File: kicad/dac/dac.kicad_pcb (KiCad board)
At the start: 4 copper layers, 100 x 99 mm, 58 parts, among them J1 USB_C_Receptacle_USB2.0, Q1 PNP, Q11 NPN, Q12 PNP, Q15 NPN, Q19 NPN, Q2 PNP, Q20 PNP, Q3 PNP, Q4 PNP, Q7 NPN, U1 PCM2704/4C/5/5C

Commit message: Commit
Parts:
- removed C1, C4, C6: 1u, Capacitor_SMD:C_0805_2012Metric_Pad1.18x1.45mm_HandSolder
- removed Q1: PNP, Package_TO_SOT_THT:TO-92L_Inline
- removed R33: 234, Resistor_THT:R_Axial_DIN0207_L6.3mm_D2.5mm_P10.16mm_Horizontal
- removed R6: R, Resistor_SMD:R_0805_2012Metric_Pad1.20x1.40mm_HandSolder
- added C10: 100n, Capacitor_SMD:C_1206_3216Metric_Pad1.33x1.80mm_HandSolder, F.Cu at (173.3, 74.0)
- added C11: 20n, Capacitor_SMD:C_1206_3216Metric_Pad1.33x1.80mm_HandSolder, F.Cu at (173.3, 77.3)
- added C12: 20n, Capacitor_SMD:C_1206_3216Metric_Pad1.33x1.80mm_HandSolder, F.Cu at (173.3, 80.7)
- added C13: 10u, Capacitor_SMD:C_1206_3216Metric_Pad1.33x1.80mm_HandSolder, F.Cu at (173.3, 84.0)
- added C14: 10u, Capacitor_SMD:C_1206_3216Metric_Pad1.33x1.80mm_HandSolder, F.Cu at (173.3, 87.4)
- added C18: 30pF, Capacitor_SMD:C_1206_3216Metric_Pad1.33x1.80mm_HandSolder, F.Cu at (159.1, 74.6)
- added C19: 10u, Capacitor_THT:CP_Radial_D5.0mm_P2.50mm, F.Cu at (139.3, 105.1)
- added C26: 30pF, Capacitor_SMD:C_1206_3216Metric_Pad1.33x1.80mm_HandSolder, F.Cu at (159.1, 19.6)
- added C27: 10u, Capacitor_THT:CP_Radial_D5.0mm_P2.50mm, F.Cu at (126.2, 44.9)
- added C3: 2u2, Capacitor_SMD:C_1206_3216Metric_Pad1.33x1.80mm_HandSolder, F.Cu at (173.3, 60.6)
- added C7: 100n, Capacitor_SMD:C_1206_3216Metric_Pad1.33x1.80mm_HandSolder, F.Cu at (173.3, 67.3)
- added C8: 2u2, Capacitor_SMD:C_1206_3216Metric_Pad1.33x1.80mm_HandSolder, F.Cu at (173.3, 70.6)
- added Q10: PNP, Package_SO:SC-74-6_1.5x2.9mm_P0.95mm, F.Cu at (165.2, 66.7)
- added Q16: PNP, Package_TO_SOT_THT:TO-220-3_Vertical, F.Cu at (158.3, 108.2)
- added Q17: PNP, Package_SO:SC-74-6_1.5x2.9mm_P0.95mm, F.Cu at (165.2, 2.80)
- added Q18: PNP, Package_SO:TSOP-6_1.65x3.05mm_P0.95mm, F.Cu at (164.3, 20.2)
- added Q21: PNP, Package_SO:SC-74-6_1.5x2.9mm_P0.95mm, F.Cu at (165.2, 11.7)
- added Q22: NPN, Package_TO_SOT_THT:TO-92, F.Cu at (158.0, 9.62)
- added Q23: NPN, Package_TO_SOT_THT:TO-92, F.Cu at (158.0, 15.4)
- added Q26: NPN, Package_TO_SOT_THT:TO-220-3_Vertical, F.Cu at (115.7, 45.5)
- added Q27: PNP, Package_TO_SOT_THT:TO-220-3_Vertical, F.Cu at (115.7, 51.5)
- added Q5: PNP, Package_TO_SOT_THT:TO-92, F.Cu at (178.3, 92.6)
- added Q6: PNP, Package_SO:SC-74-6_1.5x2.9mm_P0.95mm, F.Cu at (165.2, 57.8)
- added Q8: NPN, Package_SO:SC-74-6_1.5x2.9mm_P0.95mm, F.Cu at (165.2, 62.2)
- added Q9: NPN, Package_TO_SOT_THT:TO-92, F.Cu at (158.0, 58.8)
- added R27: 2k, Resistor_THT:R_Axial_DIN0207_L6.3mm_D2.5mm_P10.16mm_Horizontal, F.Cu at (156.6, 92.2)
- added R28: 20k, Resistor_THT:R_Axial_DIN0207_L6.3mm_D2.5mm_P10.16mm_Horizontal, F.Cu at (156.6, 96.3)
- added R41: 68, Resistor_THT:R_Axial_DIN0207_L6.3mm_D2.5mm_P10.16mm_Horizontal, F.Cu at (156.6, 29.1)
- added R42: 20k, Resistor_THT:R_Axial_DIN0207_L6.3mm_D2.5mm_P10.16mm_Horizontal, F.Cu at (156.6, 33.2)
- added R43: 27k, Resistor_SMD:R_1206_3216Metric_Pad1.30x1.75mm_HandSolder, F.Cu at (140.2, 28.8)
- added R44: 470, Resistor_SMD:R_1206_3216Metric_Pad1.30x1.75mm_HandSolder, F.Cu at (140.2, 32.1)
- added R45: 430, Resistor_SMD:R_1206_3216Metric_Pad1.30x1.75mm_HandSolder, F.Cu at (140.2, 35.4)
- added R46: 68, Resistor_SMD:R_1206_3216Metric_Pad1.30x1.75mm_HandSolder, F.Cu at (140.2, 38.6)
- added R47: 680, Resistor_SMD:R_1206_3216Metric_Pad1.30x1.75mm_HandSolder, F.Cu at (140.2, 41.9)
- added R48: 68, Resistor_SMD:R_1206_3216Metric_Pad1.30x1.75mm_HandSolder, F.Cu at (140.2, 45.2)
- added R49: 430, Resistor_SMD:R_1206_3216Metric_Pad1.30x1.75mm_HandSolder, F.Cu at (146.1, 28.8)
- added R50: 470, Resistor_SMD:R_1206_3216Metric_Pad1.30x1.75mm_HandSolder, F.Cu at (146.1, 32.1)
- added R51: 2k, Resistor_THT:R_Axial_DIN0207_L6.3mm_D2.5mm_P10.16mm_Horizontal, F.Cu at (156.6, 37.2)
- added R52: 20k, Resistor_THT:R_Axial_DIN0207_L6.3mm_D2.5mm_P10.16mm_Horizontal, F.Cu at (156.6, 41.3)
- added R53: 27k, Resistor_SMD:R_1206_3216Metric_Pad1.30x1.75mm_HandSolder, F.Cu at (146.1, 35.4)
- added R54: 2k2, Resistor_SMD:R_1206_3216Metric_Pad1.30x1.75mm_HandSolder, F.Cu at (146.1, 38.6)
- added R55: 2k2, Resistor_SMD:R_1206_3216Metric_Pad1.30x1.75mm_HandSolder, F.Cu at (146.1, 41.9)
- added R56: 680, Resistor_SMD:R_1206_3216Metric_Pad1.30x1.75mm_HandSolder, F.Cu at (146.1, 45.2)
- added R58: 68, Resistor_SMD:R_1206_3216Metric_Pad1.30x1.75mm_HandSolder, F.Cu at (152.1, 28.8)
- added R59: 100, Resistor_SMD:R_1206_3216Metric_Pad1.30x1.75mm_HandSolder, F.Cu at (152.1, 32.1)
- added R60: 22, Resistor_SMD:R_1206_3216Metric_Pad1.30x1.75mm_HandSolder, F.Cu at (152.1, 35.4)
- added R61: 33, Resistor_SMD:R_1206_3216Metric_Pad1.30x1.75mm_HandSolder, F.Cu at (152.1, 38.6)
- added R62: 33, Resistor_SMD:R_1206_3216Metric_Pad1.30x1.75mm_HandSolder, F.Cu at (152.1, 41.9)
- added R63: 1, Resistor_THT:R_Axial_DIN0614_L14.3mm_D5.7mm_P20.32mm_Horizontal, F.Cu at (114.7, 30.8)
- added R64: 1, Resistor_THT:R_Axial_DIN0614_L14.3mm_D5.7mm_P20.32mm_Horizontal, F.Cu at (114.7, 38.0)
- C2: value 1u -> 100n; footprint Capacitor_SMD:C_0805_2012Metric_Pad1.18x1.45mm_HandSolder -> Capacitor_SMD:C_1206_3216Metric_Pad1.33x1.80mm_HandSolder
- C5: value 1u -> 2u2; footprint Capacitor_SMD:C_0805_2012Metric_Pad1.18x1.45mm_HandSolder -> Capacitor_SMD:C_1206_3216Metric_Pad1.33x1.80mm_HandSolder
- HS1, HS2: footprint Heatsink:Heatsink_Fischer_SK104-STCB_35x13mm__2xDrill3.5mm_ScrewM3 -> Heatsink:Heatsink_Fischer_SK129-STS_42x25mm_2xDrill2.5mm
- J1: value USB_C_Receptacle_USB2.0 -> Conn_01x09_Pin; footprint Connector_USB:USB_C_Receptacle_GCT_USB4085 -> Connector_PinHeader_2.54mm:PinHeader_1x09_P2.54mm_Vertical
- Q11: footprint Package_TO_SOT_THT:TO-220-3_Vertical -> Package_TO_SOT_THT:TO-92
- Q12, Q20: value PNP -> NPN; footprint Package_TO_SOT_THT:TO-220-3_Vertical -> Package_TO_SOT_THT:TO-92
- Q15: footprint Package_TO_SOT_THT:TO-92L_Inline -> Package_TO_SOT_THT:TO-220-3_Vertical
- Q19: footprint Package_TO_SOT_THT:TO-220-3_Vertical -> Package_SO:SC-74-6_1.5x2.9mm_P0.95mm
- Q2, Q3, Q4: footprint Package_TO_SOT_THT:TO-92L_Inline -> Package_TO_SOT_THT:TO-92
- Q7: value NPN -> PNP; footprint Package_TO_SOT_THT:TO-92L_Inline -> Package_SO:TSOP-6_1.65x3.05mm_P0.95mm
- R1: value 1k5 -> 16; footprint Resistor_SMD:R_0805_2012Metric_Pad1.20x1.40mm_HandSolder -> Resistor_SMD:R_1206_3216Metric_Pad1.30x1.75mm_HandSolder
- R10: value 22 -> 56k; footprint Resistor_SMD:R_0805_2012Metric_Pad1.20x1.40mm_HandSolder -> Resistor_SMD:R_1206_3216Metric_Pad1.30x1.75mm_HandSolder
- R11: value 22 -> 500; footprint Resistor_SMD:R_0805_2012Metric_Pad1.20x1.40mm_HandSolder -> Resistor_SMD:R_1206_3216Metric_Pad1.30x1.75mm_HandSolder
- R12: value 1k5 -> 22k; footprint Resistor_SMD:R_0805_2012Metric_Pad1.20x1.40mm_HandSolder -> Resistor_SMD:R_1206_3216Metric_Pad1.30x1.75mm_HandSolder
- R13: value 1k5 -> R; footprint Resistor_SMD:R_0805_2012Metric_Pad1.20x1.40mm_HandSolder -> Resistor_SMD:R_1206_3216Metric_Pad1.30x1.75mm_HandSolder
- R14: value 1M -> 1k5; footprint Resistor_SMD:R_0805_2012Metric_Pad1.20x1.40mm_HandSolder -> Resistor_SMD:R_1206_3216Metric_Pad1.30x1.75mm_HandSolder
- R15: value 870 -> 1k5; footprint Resistor_THT:R_Axial_DIN0207_L6.3mm_D2.5mm_P10.16mm_Horizontal -> Resistor_SMD:R_1206_3216Metric_Pad1.30x1.75mm_HandSolder
- R16: value 20k -> 1k5; footprint Resistor_THT:R_Axial_DIN0207_L6.3mm_D2.5mm_P10.16mm_Horizontal -> Resistor_SMD:R_1206_3216Metric_Pad1.30x1.75mm_HandSolder
- R17: value 1k -> 68
- R18: value 234 -> 20k
- R19: value 234 -> 27k; footprint Resistor_THT:R_Axial_DIN0207_L6.3mm_D2.5mm_P10.16mm_Horizontal -> Resistor_SMD:R_1206_3216Metric_Pad1.30x1.75mm_HandSolder
- R2: value 56k -> 16; footprint Resistor_SMD:R_0805_2012Metric_Pad1.20x1.40mm_HandSolder -> Resistor_SMD:R_1206_3216Metric_Pad1.30x1.75mm_HandSolder
- R20: value 1k -> 470; footprint Resistor_THT:R_Axial_DIN0207_L6.3mm_D2.5mm_P10.16mm_Horizontal -> Resistor_SMD:R_1206_3216Metric_Pad1.30x1.75mm_HandSolder
- R21: value 10k -> 430; footprint Resistor_THT:R_Axial_DIN0207_L6.3mm_D2.5mm_P10.16mm_Horizontal -> Resistor_SMD:R_1206_3216Metric_Pad1.30x1.75mm_HandSolder
- R22: value 1k2 -> 68; footprint Resistor_THT:R_Axial_DIN0207_L6.3mm_D2.5mm_P10.16mm_Horizontal -> Resistor_SMD:R_1206_3216Metric_Pad1.30x1.75mm_HandSolder
- R23: value 518 -> 680; footprint Resistor_THT:R_Axial_DIN0207_L6.3mm_D2.5mm_P10.16mm_Horizontal -> Resistor_SMD:R_1206_3216Metric_Pad1.30x1.75mm_HandSolder
- R24: value 22 -> 68; footprint Resistor_THT:R_Axial_DIN0207_L6.3mm_D2.5mm_P10.16mm_Horizontal -> Resistor_SMD:R_1206_3216Metric_Pad1.30x1.75mm_HandSolder
- R25: value 33 -> 430; footprint Resistor_THT:R_Axial_DIN0207_L6.3mm_D2.5mm_P10.16mm_Horizontal -> Resistor_SMD:R_1206_3216Metric_Pad1.30x1.75mm_HandSolder
- R26: value 33 -> 470; footprint Resistor_THT:R_Axial_DIN0207_L6.3mm_D2.5mm_P10.16mm_Horizontal -> Resistor_SMD:R_1206_3216Metric_Pad1.30x1.75mm_HandSolder
- R29: value 870 -> 27k; footprint Resistor_THT:R_Axial_DIN0207_L6.3mm_D2.5mm_P10.16mm_Horizontal -> Resistor_SMD:R_1206_3216Metric_Pad1.30x1.75mm_HandSolder
- R3: value 500 -> 16; footprint Resistor_SMD:R_0805_2012Metric_Pad1.20x1.40mm_HandSolder -> Resistor_SMD:R_1206_3216Metric_Pad1.30x1.75mm_HandSolder
- R30: value 20k -> 2k2; footprint Resistor_THT:R_Axial_DIN0207_L6.3mm_D2.5mm_P10.16mm_Horizontal -> Resistor_SMD:R_1206_3216Metric_Pad1.30x1.75mm_HandSolder
- R31: value 1k -> 2k2; footprint Resistor_THT:R_Axial_DIN0207_L6.3mm_D2.5mm_P10.16mm_Horizontal -> Resistor_SMD:R_1206_3216Metric_Pad1.30x1.75mm_HandSolder
- R32: value 234 -> 680; footprint Resistor_THT:R_Axial_DIN0207_L6.3mm_D2.5mm_P10.16mm_Horizontal -> Resistor_SMD:R_1206_3216Metric_Pad1.30x1.75mm_HandSolder
- R34: value 1k -> 68; footprint Resistor_THT:R_Axial_DIN0207_L6.3mm_D2.5mm_P10.16mm_Horizontal -> Resistor_SMD:R_1206_3216Metric_Pad1.30x1.75mm_HandSolder
- R35: value 10k -> 100; footprint Resistor_THT:R_Axial_DIN0207_L6.3mm_D2.5mm_P10.16mm_Horizontal -> Resistor_SMD:R_1206_3216Metric_Pad1.30x1.75mm_HandSolder
- R36: value 1k2 -> 22; footprint Resistor_THT:R_Axial_DIN0207_L6.3mm_D2.5mm_P10.16mm_Horizontal -> Resistor_SMD:R_1206_3216Metric_Pad1.30x1.75mm_HandSolder
- R37: value 518 -> 33; footprint Resistor_THT:R_Axial_DIN0207_L6.3mm_D2.5mm_P10.16mm_Horizontal -> Resistor_SMD:R_1206_3216Metric_Pad1.30x1.75mm_HandSolder
- R38: value 22 -> 33; footprint Resistor_THT:R_Axial_DIN0207_L6.3mm_D2.5mm_P10.16mm_Horizontal -> Resistor_SMD:R_1206_3216Metric_Pad1.30x1.75mm_HandSolder
- R39, R40: value 33 -> 1; footprint Resistor_THT:R_Axial_DIN0207_L6.3mm_D2.5mm_P10.16mm_Horizontal -> Resistor_THT:R_Axial_DIN0614_L14.3mm_D5.7mm_P20.32mm_Horizontal
- R4: value 22k -> 16; footprint Resistor_SMD:R_0805_2012Metric_Pad1.20x1.40mm_HandSolder -> Resistor_SMD:R_1206_3216Metric_Pad1.30x1.75mm_HandSolder
- R5: value 5.1k -> 680; footprint Resistor_SMD:R_0805_2012Metric_Pad1.20x1.40mm_HandSolder -> Resistor_SMD:R_1206_3216Metric_Pad1.30x1.75mm_HandSolder
- R7, R8: value 1k5 -> 2; footprint Resistor_SMD:R_0805_2012Metric_Pad1.20x1.40mm_HandSolder -> Resistor_SMD:R_1206_3216Metric_Pad1.30x1.75mm_HandSolder
- R9: footprint Resistor_SMD:R_0805_2012Metric_Pad1.20x1.40mm_HandSolder -> Resistor_SMD:R_1206_3216Metric_Pad1.30x1.75mm_HandSolder
- U1: value PCM2704/4C/5/5C -> PCM510xA; footprint Package_SO:SSOP-28_5.3x10.2mm_P0.65mm -> Package_SO:TSSOP-20_4.4x6.5mm_P0.65mm
- moved R29 167.1 mm to (146.1, 90.3)
- moved R30 166.7 mm to (146.1, 93.6)
- moved R31 166.4 mm to (146.1, 96.9)
- moved R32 166.0 mm to (146.1, 100.2)
- moved R34 160.6 mm to (152.1, 83.7)
- moved R35 160.4 mm to (152.1, 87.0)
- moved R36 160.1 mm to (152.1, 90.3)
- moved R37 159.8 mm to (152.1, 93.6)
- moved R38 159.5 mm to (152.1, 96.9)
- moved Q15 158.1 mm to (158.3, 102.2)
- moved Q19 148.3 mm to (165.2, 7.25)
- moved Q20 142.5 mm to (158.0, 3.83)
- moved Q7 134.1 mm to (164.3, 75.2)
- moved R15 120.6 mm to (191.2, 67.1)
- moved R40 120.3 mm to (114.7, 93.0)
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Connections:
- C2 pad 2: Net-(U1-Vccp) -> Net-(U1-LDOO)
- C5 pad 2: Net-(U1-VccR) -> Net-(U1-VNEG)
- Q11 pad 1: +36V -> Net-(Q11-C)
- Q12 pad 1: -36V -> Net-(Q11-E)
- Q12 pad 2: Net-(Q10-E) -> Net-(Q12-B)
- Q15 pad 1: Net-(Q15-C) -> +30V
- Q15 pad 2: Net-(Q15-B) -> Net-(Q13-E)
- Q19 pad 1: +36V -> Net-(Q17B-C)
- Q19 pad 2: Net-(Q17-E) -> Net-(Q17B-C)
- Q19 pad 3: Net-(Q19-E) -> Net-(Q17B-C)
- Q2 pad 1: Net-(Q2-C) -> -30V
- Q2 pad 2: Net-(Q1-E) -> Net-(Q2-B)
- Q2 pad 3: GNDA -> Net-(Q2-E)
- Q20 pad 1: -36V -> GNDA
- Q20 pad 2: Net-(Q18-E) -> Net-(Q17A-C)
- Q3 pad 2: Net-(Q3-B) -> Net-(Q2-E)
- Q4 pad 2: unconnected-(Q4-B-Pad2) -> Net-(Q4-B)
- Q7 pad 1: Net-(Q7-C) -> Net-(Q7A-B)
- Q7 pad 2: Net-(Q7-B) -> Net-(Q7A-C)
- Q7 pad 3: Net-(Q10-B) -> Net-(Q7B-C)
- R1 pad 1: Net-(Q3-B) -> Net-(C11-Pad2)
- R1 pad 2: GNDA -> /AMP_L
- R10 pad 1: Net-(D4-A2) -> -30V
- R10 pad 2: Net-(U1-D-) -> Net-(Q4-B)
- R11 pad 1: Net-(D3-A2) -> Net-(Q2-B)
- R11 pad 2: Net-(U1-D+) -> GNDA
- R12 pad 1: Net-(D6-BA) -> -30V
- R12 pad 2: Net-(Q4-C) -> Net-(Q2-B)
- R13 pad 1: Net-(U1-DT) -> GNDA
- R13 pad 2: VDD -> Net-(Q2-E)
- R14 pad 1: Net-(U1-XTI) -> Net-(D11-RA)
- R14 pad 2: Net-(U1-XTO) -> Net-(Q3-C)
- R15 pad 2: Net-(C8-Pad1) -> Net-(Q4-C)
- R16 pad 1: GNDA -> Net-(D11-BA)
- R17 pad 1: -36V -> /DAC_L
- R17 pad 2: Net-(Q5-C) (its old number) -> Net-(C16-Pad1)
- R18 pad 1: Net-(Q5-E) -> GNDA
- R18 pad 2: Net-(I1-Pad2) -> Net-(Q6A-B)
- R19 pad 1: Net-(I1-Pad2) -> GNDA
- R19 pad 2: Net-(Q6-E) -> Net-(Q7A-C)
- R2 pad 1: -36V -> Net-(C12-Pad2)
- R2 pad 2: Net-(Q3-B) -> /AMP_R
- R20 pad 1: GNDA -> -30V
- R20 pad 2: Net-(Q6-B) -> Net-(Q8A-E)
- R21 pad 1: Net-(Q6-B) -> Net-(Q6A-E)
- R21 pad 2: /amplifier_left/OUT -> Net-(R21-Pad2)
- R22 pad 1: Net-(Q7-B) -> Net-(R21-Pad2)
- R22 pad 2: Net-(Q7-C) -> Net-(Q7B-C)
- R23 pad 1: Net-(Q10-B) -> Net-(Q7A-B)
- R23 pad 2: Net-(Q7-B) -> +30V
- R24 pad 1: -36V -> Net-(R24-Pad1)
- R24 pad 2: Net-(Q8-E) -> Net-(Q7B-C)
- R25 pad 1: /amplifier_left/OUT -> Net-(R24-Pad1)
- R25 pad 2: Net-(Q11-B) -> Net-(Q6B-E)
- R26 pad 1: Net-(Q10-E) -> -30V
- R26 pad 2: /amplifier_left/OUT -> Net-(Q8B-E)
- R29 pad 1: Net-(C10-Pad1) -> GNDA
- R29 pad 2: Net-(C11-Pad1) -> Net-(Q10A-C)
- R3 pad 1: Net-(Q1-B) -> Net-(K1-Pad10)
- R30 pad 1: GNDA -> -30V
- R30 pad 2: Net-(Q13-B) -> Net-(Q12-B)
- R31 pad 1: -36V -> Net-(Q11-B)
- R31 pad 2: Net-(Q13-C) -> Net-(Q10B-C)
- R32 pad 2: Net-(I3-Pad2) -> Net-(Q11-B)
- R34 pad 1: GNDA -> Net-(Q10A-B)
- R34 pad 2: Net-(Q14-B) -> +30V
- R35 pad 1: Net-(Q14-B) -> Net-(Q10B-C)
- R35 pad 2: /amplifier_right/OUT -> Net-(Q11-C)
- R36 pad 1: Net-(Q15-B) -> -30V
- R36 pad 2: Net-(Q15-C) -> Net-(Q12-E)
- R37 pad 1: Net-(Q15-E) -> /AMP_L
- R37 pad 2: Net-(Q15-B) -> Net-(Q13-E)
- R38 pad 1: -36V -> Net-(Q14-E)
- R38 pad 2: Net-(Q16-E) -> /AMP_L
- R39 pad 1: /amplifier_right/OUT -> Net-(Q15-E)
- R39 pad 2: Net-(Q17-E) -> /AMP_L
- R4 pad 1: -36V -> Net-(K1-Pad3)
- R4 pad 2: Net-(Q1-B) -> GNDA
- R40 pad 1: Net-(Q18-E) -> /AMP_L
- R40 pad 2: /amplifier_right/OUT -> Net-(Q16-E)
- R5 pad 1: Net-(J1-CC1) -> Net-(D5-K)
- R5 pad 2: GNDA -> +30V
- R7 pad 1: Net-(D3-A2) -> Net-(C13-Pad2)
- R7 pad 2: VBUS -> /OUT_L
- R8 pad 2: Net-(Q2-C) -> /OUT_R
- R9 pad 1: Net-(D6-GA) -> Net-(Q4-B)
- R9 pad 2: Net-(Q3-C) -> GNDA
- RV1 pad 1: /amplifier_left/IN -> Net-(C16-Pad1)
- RV1 pad 2: Net-(C8-Pad1) -> Net-(C17-Pad1)
- RV1 pad 4: /amplifier_right/IN -> Net-(C24-Pad1)
- RV1 pad 5: Net-(C11-Pad1) -> Net-(C25-Pad1)
- U1 pad 1: Net-(U1-XTO) -> Net-(U1-CPVDD)
- U1 pad 10: VBUS -> GNDA
- U1 pad 12: GNDA -> /SCK
- U1 pad 13: Net-(U1-VccL) -> /BCK
- U1 pad 14: /amplifier_left/IN -> /DATA
- U1 pad 15: /amplifier_right/IN -> /LRCK
- U1 pad 16: Net-(U1-VccR) -> GNDA
- U1 pad 17: GNDA -> /SSPND
- U1 pad 18: Net-(U1-Vcom) -> Net-(U1-LDOO)
- U1 pad 2: unconnected-(U1-CK-Pad2) -> Net-(U1-CAPP)
- U1 pad 20: Net-(U1-Vccp) -> +3V3
- U1 pad 3: Net-(U1-DT) -> GNDA
- U1 pad 4: VDD -> Net-(U1-CAPM)
- U1 pad 5: unconnected-(U1-DOUT-Pad5) -> Net-(U1-VNEG)
- U1 pad 6: GNDA -> /DAC_L
- U1 pad 7: VDD -> /DAC_R
- U1 pad 8: Net-(U1-D-) -> Net-(U1-AVDD)
- U1 pad 9: Net-(U1-D+) -> GNDA

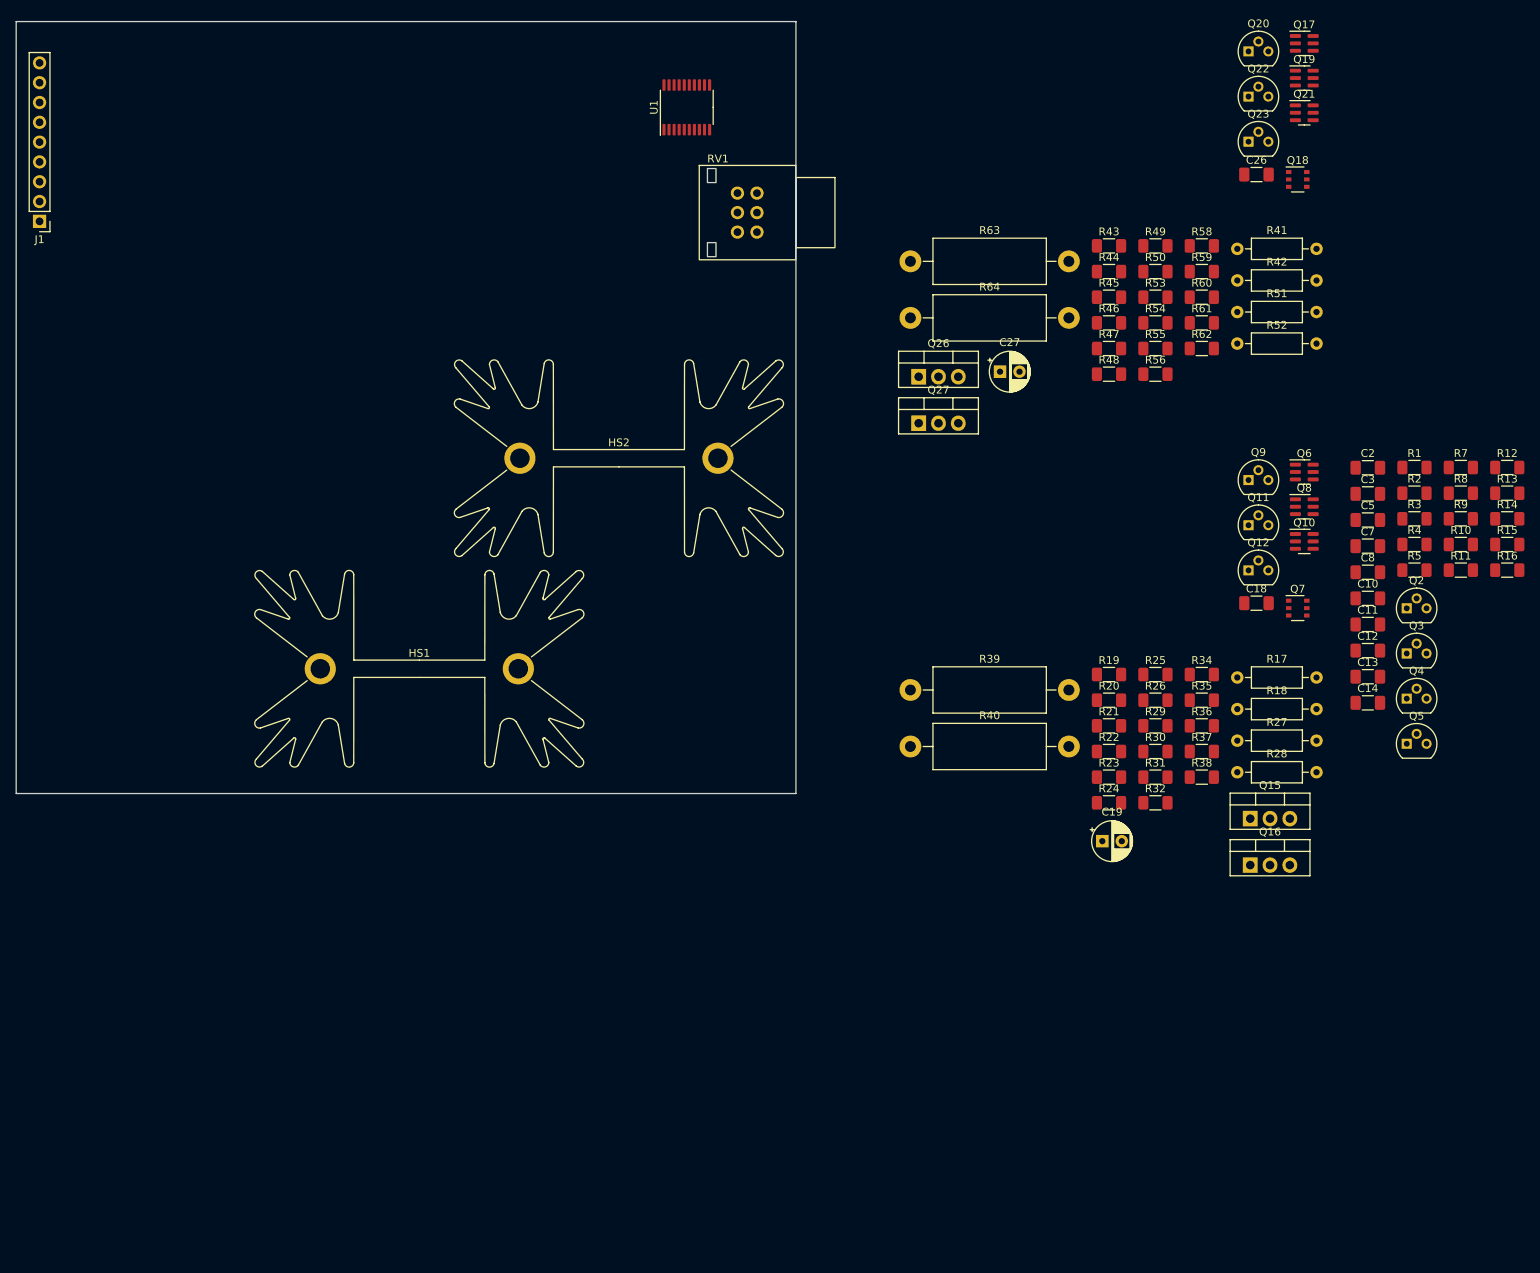
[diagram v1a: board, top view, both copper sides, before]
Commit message: completed power supply footprints and placement
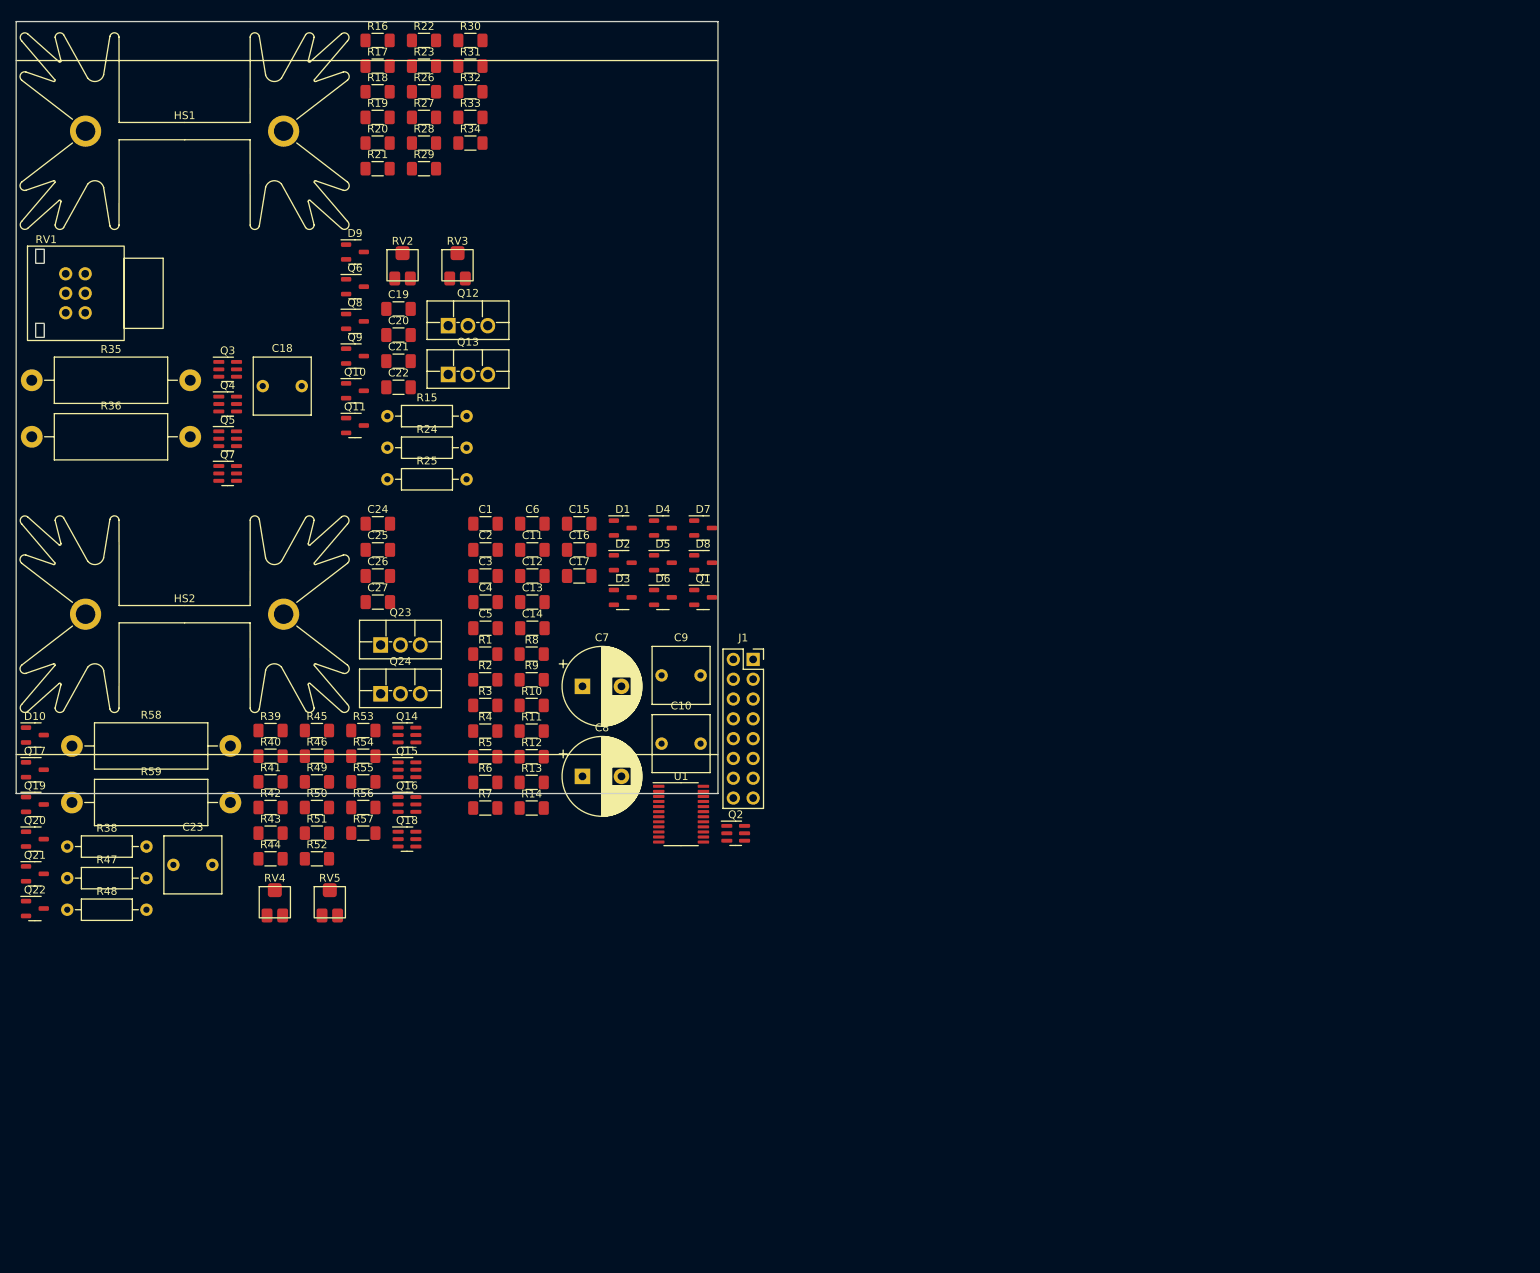
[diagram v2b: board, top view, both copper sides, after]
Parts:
- removed Q26: NPN, Package_TO_SOT_THT:TO-220-3_Vertical
- removed Q27: PNP, Package_TO_SOT_THT:TO-220-3_Vertical
- removed R37, R61, R62: 33, Resistor_SMD:R_1206_3216Metric_Pad1.30x1.75mm_HandSolder
- removed R60: 22, Resistor_SMD:R_1206_3216Metric_Pad1.30x1.75mm_HandSolder
- removed R63, R64: 1, Resistor_THT:R_Axial_DIN0614_L14.3mm_D5.7mm_P20.32mm_Horizontal
- added C1: 10u, Capacitor_SMD:C_1206_3216Metric_Pad1.33x1.80mm_HandSolder, F.Cu at (60.2, 64.4)
- added C15: 20n, Capacitor_SMD:C_1206_3216Metric_Pad1.33x1.80mm_HandSolder, F.Cu at (72.2, 64.4)
- added C16: 10u, Capacitor_SMD:C_1206_3216Metric_Pad1.33x1.80mm_HandSolder, F.Cu at (72.2, 67.8)
- added C17: 10u, Capacitor_SMD:C_1206_3216Metric_Pad1.33x1.80mm_HandSolder, F.Cu at (72.2, 71.1)
- added C20: 10u, Capacitor_SMD:C_1206_3216Metric_Pad1.33x1.80mm_HandSolder, F.Cu at (49.0, 40.2)
- added C21: 10u, Capacitor_SMD:C_1206_3216Metric_Pad1.33x1.80mm_HandSolder, F.Cu at (49.0, 43.5)
- added C22: 10u, Capacitor_SMD:C_1206_3216Metric_Pad1.33x1.80mm_HandSolder, F.Cu at (49.0, 46.9)
- added C23: 3u3, Capacitor_THT:C_Rect_L7.2mm_W7.2mm_P5.00mm_FKS2_FKP2_MKS2_MKP2, F.Cu at (20.2, 108.2)
- added C24: 30p, Capacitor_SMD:C_1206_3216Metric_Pad1.33x1.80mm_HandSolder, F.Cu at (46.4, 64.4)
- added C25: 10u, Capacitor_SMD:C_1206_3216Metric_Pad1.33x1.80mm_HandSolder, F.Cu at (46.4, 67.8)
- added C4: 10u, Capacitor_SMD:C_1206_3216Metric_Pad1.33x1.80mm_HandSolder, F.Cu at (60.2, 74.5)
- added C6: 10u, Capacitor_SMD:C_1206_3216Metric_Pad1.33x1.80mm_HandSolder, F.Cu at (66.2, 64.4)
- added C9: 3u3, Capacitor_THT:C_Rect_L7.2mm_W7.2mm_P5.00mm_FKS2_FKP2_MKS2_MKP2, F.Cu at (82.8, 83.8)
- added D1: ~, Package_TO_SOT_SMD:SOT-23-3, F.Cu at (77.8, 65.0)
- added D10: ~, Package_TO_SOT_SMD:SOT-23-3, F.Cu at (2.40, 91.5)
- added D2: ~, Package_TO_SOT_SMD:SOT-23-3, F.Cu at (77.8, 69.4)
- added D3: ~, Package_TO_SOT_SMD:SOT-23-3, F.Cu at (77.8, 73.8)
- added D4: ~, Package_TO_SOT_SMD:SOT-23-3, F.Cu at (82.9, 65.0)
- added D5: ~, Package_TO_SOT_SMD:SOT-23-3, F.Cu at (82.9, 69.4)
- added D6: ~, Package_TO_SOT_SMD:SOT-23-3, F.Cu at (82.9, 73.8)
- added D7: ~, Package_TO_SOT_SMD:SOT-23-3, F.Cu at (88.1, 65.0)
- added D8: ~, Package_TO_SOT_SMD:SOT-23-3, F.Cu at (88.1, 69.4)
- added D9: ~, Package_TO_SOT_SMD:SOT-23-3, F.Cu at (43.5, 29.6)
- added Q1: MMBT5551, Package_TO_SOT_SMD:SOT-23-3, F.Cu at (88.1, 73.8)
- added Q13: 2SA1725, Package_TO_SOT_THT:TO-220F-3_Vertical, F.Cu at (55.4, 45.3)
- added Q14: BCM53DS, Package_SO:SC-74-6_1.5x2.9mm_P0.95mm, F.Cu at (50.1, 91.5)
- added Q24: 2SA1725, Package_TO_SOT_THT:TO-220F-3_Vertical, F.Cu at (46.7, 86.2)
- added R33: 33, Resistor_SMD:R_1206_3216Metric_Pad1.30x1.75mm_HandSolder, F.Cu at (58.2, 12.3)
- added R57: 33, Resistor_SMD:R_1206_3216Metric_Pad1.30x1.75mm_HandSolder, F.Cu at (44.5, 104.1)
- added R6: 10k, Resistor_SMD:R_1206_3216Metric_Pad1.30x1.75mm_HandSolder, F.Cu at (60.2, 97.6)
- added RV2: 100, library:TC33, F.Cu at (49.5, 31.1)
- added RV3: 500, library:TC33, F.Cu at (56.6, 31.1)
- added RV4: 100, library:TC33, F.Cu at (33.2, 112.8)
- added RV5: 500, library:TC33, F.Cu at (40.2, 112.8)
- C10: value 100n -> 3u3; footprint Capacitor_SMD:C_1206_3216Metric_Pad1.33x1.80mm_HandSolder -> Capacitor_THT:C_Rect_L7.2mm_W7.2mm_P5.00mm_FKS2_FKP2_MKS2_MKP2
- C11: value 20n -> 100n
- C12: value 20n -> 10u
- C14: value 10u -> 20n
- C18: value 30pF -> 3u3; footprint Capacitor_SMD:C_1206_3216Metric_Pad1.33x1.80mm_HandSolder -> Capacitor_THT:C_Rect_L7.2mm_W7.2mm_P5.00mm_FKS2_FKP2_MKS2_MKP2
- C19: value 10u -> 30p; footprint Capacitor_THT:CP_Radial_D5.0mm_P2.50mm -> Capacitor_SMD:C_1206_3216Metric_Pad1.33x1.80mm_HandSolder
- C2: value 100n -> 10u
- C26: value 30pF -> 10u
- C27: footprint Capacitor_THT:CP_Radial_D5.0mm_P2.50mm -> Capacitor_SMD:C_1206_3216Metric_Pad1.33x1.80mm_HandSolder
- C3: value 2u2 -> 100n
- C5: value 2u2 -> 3u3
- C7: value 100n -> 470u; footprint Capacitor_SMD:C_1206_3216Metric_Pad1.33x1.80mm_HandSolder -> Capacitor_THT:CP_Radial_D10.0mm_P5.00mm
- C8: value 2u2 -> 470u; footprint Capacitor_SMD:C_1206_3216Metric_Pad1.33x1.80mm_HandSolder -> Capacitor_THT:CP_Radial_D10.0mm_P5.00mm
- J1: value Conn_01x09_Pin -> Conn_02x08_Odd_Even; footprint Connector_PinHeader_2.54mm:PinHeader_1x09_P2.54mm_Vertical -> Connector_PinSocket_2.54mm:PinSocket_2x08_P2.54mm_Vertical
- Q10, Q17, Q21, Q6: value PNP -> MMBT5551; footprint Package_SO:SC-74-6_1.5x2.9mm_P0.95mm -> Package_TO_SOT_SMD:SOT-23-3
- Q11, Q22: value NPN -> MMBT5401; footprint Package_TO_SOT_THT:TO-92 -> Package_TO_SOT_SMD:SOT-23-3
- Q12, Q23: value NPN -> 2SC4511; footprint Package_TO_SOT_THT:TO-92 -> Package_TO_SOT_THT:TO-220F-3_Vertical
- Q15: value NPN -> BCM53DS; footprint Package_TO_SOT_THT:TO-220-3_Vertical -> Package_SO:SC-74-6_1.5x2.9mm_P0.95mm
- Q16: value PNP -> BCM56DS; footprint Package_TO_SOT_THT:TO-220-3_Vertical -> Package_SO:SC-74-6_1.5x2.9mm_P0.95mm
- Q18, Q7: value PNP -> BCM53DS; footprint Package_SO:TSOP-6_1.65x3.05mm_P0.95mm -> Package_SO:SC-74-6_1.5x2.9mm_P0.95mm
- Q19, Q8: value NPN -> MMBT5551; footprint Package_SO:SC-74-6_1.5x2.9mm_P0.95mm -> Package_TO_SOT_SMD:SOT-23-3
- Q2, Q3, Q4: value PNP -> BCM53DS; footprint Package_TO_SOT_THT:TO-92 -> Package_SO:SC-74-6_1.5x2.9mm_P0.95mm
- Q20, Q9: value NPN -> MMBT5551; footprint Package_TO_SOT_THT:TO-92 -> Package_TO_SOT_SMD:SOT-23-3
- Q5: value PNP -> BCM56DS; footprint Package_TO_SOT_THT:TO-92 -> Package_SO:SC-74-6_1.5x2.9mm_P0.95mm
- R1: value 16 -> 47k
- R10: value 56k -> 10k
- R11: value 500 -> 16
- R12: value 22k -> 16
- R13: value R -> 2
- R14: value 1k5 -> 2
- R15: value 1k5 -> 20k; footprint Resistor_SMD:R_1206_3216Metric_Pad1.30x1.75mm_HandSolder -> Resistor_THT:R_Axial_DIN0207_L6.3mm_D2.5mm_P10.16mm_Horizontal
- R16: value 1k5 -> 27k
- R17, R41: value 68 -> 430; footprint Resistor_THT:R_Axial_DIN0207_L6.3mm_D2.5mm_P10.16mm_Horizontal -> Resistor_SMD:R_1206_3216Metric_Pad1.30x1.75mm_HandSolder
- R18, R52: value 20k -> 430; footprint Resistor_THT:R_Axial_DIN0207_L6.3mm_D2.5mm_P10.16mm_Horizontal -> Resistor_SMD:R_1206_3216Metric_Pad1.30x1.75mm_HandSolder
- R19, R53: value 27k -> 68
- R2, R3: value 16 -> 100k
- R20: value 470 -> 680
- R21: value 430 -> 68
- R22, R46: value 68 -> 430
- R23: value 680 -> 430
- R24: value 68 -> 2k5; footprint Resistor_SMD:R_1206_3216Metric_Pad1.30x1.75mm_HandSolder -> Resistor_THT:R_Axial_DIN0207_L6.3mm_D2.5mm_P10.16mm_Horizontal
- R25: value 430 -> 20k; footprint Resistor_SMD:R_1206_3216Metric_Pad1.30x1.75mm_HandSolder -> Resistor_THT:R_Axial_DIN0207_L6.3mm_D2.5mm_P10.16mm_Horizontal
- R26: value 470 -> 2k2
- R27: value 2k -> 27k; footprint Resistor_THT:R_Axial_DIN0207_L6.3mm_D2.5mm_P10.16mm_Horizontal -> Resistor_SMD:R_1206_3216Metric_Pad1.30x1.75mm_HandSolder
- R28: value 20k -> 2k2; footprint Resistor_THT:R_Axial_DIN0207_L6.3mm_D2.5mm_P10.16mm_Horizontal -> Resistor_SMD:R_1206_3216Metric_Pad1.30x1.75mm_HandSolder
- R29: value 27k -> 430
- R30: value 2k2 -> 68
- R31, R54: value 2k2 -> 12
- R32: value 680 -> 22
- R34: value 68 -> 33
- R35, R59: value 100 -> 1; footprint Resistor_SMD:R_1206_3216Metric_Pad1.30x1.75mm_HandSolder -> Resistor_THT:R_Axial_DIN0614_L14.3mm_D5.7mm_P20.32mm_Horizontal
- R36: value 22 -> 1; footprint Resistor_SMD:R_1206_3216Metric_Pad1.30x1.75mm_HandSolder -> Resistor_THT:R_Axial_DIN0614_L14.3mm_D5.7mm_P20.32mm_Horizontal
- R38: value 33 -> 20k; footprint Resistor_SMD:R_1206_3216Metric_Pad1.30x1.75mm_HandSolder -> Resistor_THT:R_Axial_DIN0207_L6.3mm_D2.5mm_P10.16mm_Horizontal
- R39: value 1 -> 27k; footprint Resistor_THT:R_Axial_DIN0614_L14.3mm_D5.7mm_P20.32mm_Horizontal -> Resistor_SMD:R_1206_3216Metric_Pad1.30x1.75mm_HandSolder
- R40: value 1 -> 430; footprint Resistor_THT:R_Axial_DIN0614_L14.3mm_D5.7mm_P20.32mm_Horizontal -> Resistor_SMD:R_1206_3216Metric_Pad1.30x1.75mm_HandSolder
- R42: value 20k -> 68; footprint Resistor_THT:R_Axial_DIN0207_L6.3mm_D2.5mm_P10.16mm_Horizontal -> Resistor_SMD:R_1206_3216Metric_Pad1.30x1.75mm_HandSolder
- R43: value 27k -> 680
- R44: value 470 -> 68
- R47: value 680 -> 2k5; footprint Resistor_SMD:R_1206_3216Metric_Pad1.30x1.75mm_HandSolder -> Resistor_THT:R_Axial_DIN0207_L6.3mm_D2.5mm_P10.16mm_Horizontal
- R48: value 68 -> 20k; footprint Resistor_SMD:R_1206_3216Metric_Pad1.30x1.75mm_HandSolder -> Resistor_THT:R_Axial_DIN0207_L6.3mm_D2.5mm_P10.16mm_Horizontal
- R49: value 430 -> 2k2
- R5: value 680 -> 16
- R50: value 470 -> 27k
- R51: value 2k -> 2k2; footprint Resistor_THT:R_Axial_DIN0207_L6.3mm_D2.5mm_P10.16mm_Horizontal -> Resistor_SMD:R_1206_3216Metric_Pad1.30x1.75mm_HandSolder
- R55: value 2k2 -> 22
- R56: value 680 -> 33
- R58: value 68 -> 1; footprint Resistor_SMD:R_1206_3216Metric_Pad1.30x1.75mm_HandSolder -> Resistor_THT:R_Axial_DIN0614_L14.3mm_D5.7mm_P20.32mm_Horizontal
- R7: value 2 -> 10k
- R8: value 2 -> 100k
- R9: value 1k5 -> 10k
- U1: value PCM510xA -> CS4349; footprint Package_SO:TSSOP-20_4.4x6.5mm_P0.65mm -> Package_SO:TSSOP-24_4.4x7.8mm_P0.65mm
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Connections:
- C10 pad 1: Net-(U1-AVDD) -> -25V
- C10 pad 2: GNDA -> GND
- C11 pad 1: GNDA -> Net-(U1-VD_FILT)
- C11 pad 2: Net-(C11-Pad2) -> GND
- C12 pad 1: GNDA -> /DC_LP_L
- C12 pad 2: Net-(C12-Pad2) -> GND
- C13 pad 1: /AMP_L -> /DC_LP_R
- C13 pad 2: Net-(C13-Pad2) -> GND
- C14 pad 1: /AMP_R -> GND
- C18 pad 1: Net-(Q6A-C) -> Net-(C18-Pad1)
- C18 pad 2: Net-(Q11-E) -> Net-(Q3A-B)
- C19 pad 1: Net-(Q11-C) -> Net-(Q3A-C)
- C19 pad 2: Net-(Q11-E) -> /amplifier_left/V_{bias}-
- C2 pad 1: GNDA -> GND
- C2 pad 2: Net-(U1-LDOO) -> VBUS
- C26 pad 1: Net-(Q17A-C) -> +20Vreg
- C26 pad 2: Net-(Q22-E) -> GND
- C27 pad 1: Net-(Q22-C) -> GND
- C27 pad 2: Net-(Q22-E) -> -20Vreg
- C3 pad 1: Net-(U1-CPVDD) -> VBUS
- C3 pad 2: GNDA -> GND
- C5 pad 1: GNDA -> Net-(U1-VQ)
- C5 pad 2: Net-(U1-VNEG) -> GND
- C7 pad 1: GNDA -> +25V
- C7 pad 2: +3V3 -> GND
- C8 pad 1: Net-(U1-CAPP) -> GND
- C8 pad 2: Net-(U1-CAPM) -> -25V
- J1 pad 1: +30V -> +20Vreg
- J1 pad 2: -30V -> +25V
- J1 pad 3: GNDA -> GND
- J1 pad 4: +3V3 -> GND
- J1 pad 5: /LRCK -> -20Vreg
- J1 pad 6: /BCK -> -25V
- J1 pad 7: /SCK -> unconnected-(J1-Pin_7-Pad7)
- J1 pad 8: /DATA -> unconnected-(J1-Pin_8-Pad8)
- J1 pad 9: /SSPND -> VBUS
- Q10 pad 1: Net-(Q10A-B) -> /amplifier_left/V_{bias}+
- Q10 pad 2: Net-(Q10A-C) -> /amplifier_left/V_{OPS}+
- Q10 pad 3: Net-(Q10B-C) -> +25V
- Q11 pad 1: Net-(Q11-C) -> /amplifier_left/V_{bias}-
- Q11 pad 2: Net-(Q11-B) -> /amplifier_left/V_{OPS}-
- Q11 pad 3: Net-(Q11-E) -> -25V
- Q12 pad 1: Net-(Q11-E) -> /amplifier_left/V_{OPS}+
- Q12 pad 2: Net-(Q12-B) -> +25V
- Q12 pad 3: Net-(Q12-E) -> /amplifier_left/V_{q}+
- Q15 pad 1: +30V -> Net-(Q15A-B)
- Q15 pad 2: Net-(Q13-E) -> Net-(Q15A-C)
- Q15 pad 3: Net-(Q15-E) -> /amplifier_right/CC_IPS
- Q16 pad 1: -30V -> /amplifier_right/CM
- Q16 pad 2: Net-(Q14-E) -> /amplifier_right/CM
- Q16 pad 3: Net-(Q16-E) -> /amplifier_right/CM
- Q17 pad 1: Net-(Q17A-B) -> Net-(Q14A-C)
- Q17 pad 2: Net-(Q17B-B) -> Net-(Q17-E)
- Q17 pad 3: Net-(Q17B-C) -> GND
- Q18 pad 3: Net-(Q18B-C) -> /amplifier_right/CC_VAS
- Q18 pad 5: +30V -> +20Vreg
- Q19 pad 1: Net-(Q17B-C) -> /amplifier_right/V_{bias}B
- Q19 pad 2: Net-(Q17B-C) -> /amplifier_right/V_{bias}-
- Q19 pad 3: Net-(Q17B-C) -> /amplifier_right/V_{bias}+
- Q2 pad 1: -30V -> Net-(Q2A-B)
- Q2 pad 2: Net-(Q2-B) -> Net-(D1-A)
- Q2 pad 3: Net-(Q2-E) -> Net-(Q1-E)
- Q20 pad 1: GNDA -> Net-(Q17-E)
- Q20 pad 2: Net-(Q17A-C) -> Net-(Q20-E)
- Q20 pad 3: Net-(Q20-E) -> /amplifier_right/V_{bias}-
- Q21 pad 1: Net-(Q21A-B) -> /amplifier_right/V_{bias}+
- Q21 pad 2: Net-(Q21A-C) -> /amplifier_right/V_{OPS}+
- Q21 pad 3: Net-(Q21B-C) -> +25V
- Q22 pad 1: Net-(Q22-C) -> /amplifier_right/V_{bias}-
- Q22 pad 2: Net-(Q22-B) -> /amplifier_right/V_{OPS}-
- Q22 pad 3: Net-(Q22-E) -> -25V
- Q23 pad 1: Net-(Q22-E) -> /amplifier_right/V_{OPS}+
- Q23 pad 2: Net-(Q20-E) -> +25V
- Q23 pad 3: Net-(Q23-E) -> /amplifier_right/V_{q}+
- Q3 pad 1: Net-(Q3-C) -> Net-(Q3A-B)
- Q3 pad 2: Net-(Q2-E) -> /amplifier_left/FB
- Q3 pad 3: GNDA -> /amplifier_left/CM
- Q4 pad 1: Net-(Q4-C) -> Net-(Q4A-B)
- Q4 pad 2: Net-(Q4-B) -> Net-(Q4A-C)
- Q4 pad 3: GNDA -> /amplifier_left/CC_IPS
- Q5 pad 1: Net-(Q5-C) -> /amplifier_left/CM
- Q5 pad 2: unconnected-(Q5-B-Pad2) -> /amplifier_left/CM
- Q5 pad 3: GNDA -> /amplifier_left/CM
- Q6 pad 1: Net-(Q6A-B) -> Net-(Q3A-C)
- Q6 pad 2: Net-(Q6B-B) -> Net-(Q6-E)
- Q6 pad 3: Net-(Q6B-C) -> GND
- Q7 pad 3: Net-(Q7B-C) -> /amplifier_left/CC_VAS
- Q7 pad 5: +30V -> +20Vreg
- Q8 pad 1: Net-(Q6B-C) -> /amplifier_left/V_{bias}B
- Q8 pad 2: Net-(Q6B-C) -> /amplifier_left/V_{bias}-
- Q8 pad 3: Net-(Q6B-C) -> /amplifier_left/V_{bias}+
- Q9 pad 1: GNDA -> Net-(Q6-E)
- Q9 pad 2: Net-(Q6A-C) -> Net-(Q9-E)
- Q9 pad 3: Net-(Q12-B) -> /amplifier_left/V_{bias}-
- R1 pad 1: Net-(C11-Pad2) -> Net-(U1-POPGUARD/TSTO)
- R1 pad 2: /AMP_L -> VBUS
- R10 pad 1: -30V -> Net-(Q2B-E)
- R10 pad 2: Net-(Q4-B) -> unconnected-(R10-Pad2)
- R11 pad 1: Net-(Q2-B) -> Net-(K1-Pad10)
- R11 pad 2: GNDA -> GND
- R12 pad 1: -30V -> Net-(K1-Pad3)
- R12 pad 2: Net-(Q2-B) -> GND
- R13 pad 1: GNDA -> Net-(C16-Pad2)
- R13 pad 2: Net-(Q2-E) -> /OUT_L
- R14 pad 2: Net-(Q3-C) -> /OUT_R
- R15 pad 1: Net-(D11-GA) -> GND
- R15 pad 2: Net-(Q4-C) -> Net-(Q3A-B)
- R16 pad 1: Net-(D11-BA) -> GND
- R16 pad 2: Net-(Q5-C) -> Net-(Q4A-C)
- R17 pad 1: /DAC_L -> -20Vreg
- R17 pad 2: Net-(C16-Pad1) -> Net-(Q5A-E)
- R18 pad 1: GNDA -> Net-(Q3A-E)
- R18 pad 2: Net-(Q6A-B) -> Net-(R18-Pad2)
- R19 pad 1: GNDA -> Net-(R18-Pad2)
- R19 pad 2: Net-(Q7A-C) -> /amplifier_left/CC_IPS
- R2 pad 1: Net-(C12-Pad2) -> /OUT_L
- R2 pad 2: /AMP_R -> /DC_LP_L
- R20 pad 1: -30V -> Net-(Q4A-B)
- R20 pad 2: Net-(Q8A-E) -> +20Vreg
- R21 pad 1: Net-(Q6A-E) -> Net-(R21-Pad1)
- R21 pad 2: Net-(R21-Pad2) -> /amplifier_left/CC_IPS
- R22 pad 1: Net-(R21-Pad2) -> Net-(R21-Pad1)
- R22 pad 2: Net-(Q7B-C) -> Net-(Q3B-E)
- R23 pad 1: Net-(Q7A-B) -> -20Vreg
- R23 pad 2: +30V -> Net-(Q5B-E)
- R24 pad 1: Net-(R24-Pad1) -> GND
- R24 pad 2: Net-(Q7B-C) -> /amplifier_left/FB
- R25 pad 1: Net-(R24-Pad1) -> /amplifier_left/FB
- R25 pad 2: Net-(Q6B-E) -> /AMP_L
- R26 pad 1: -30V -> -20Vreg
- R26 pad 2: Net-(Q8B-E) -> Net-(Q6-E)
- R27 pad 1: GNDA -> GND
- R27 pad 2: Net-(Q6B-B) -> Net-(Q7A-C)
- R28 pad 1: Net-(Q6B-B) -> /amplifier_left/V_{bias}B
- R28 pad 2: /AMP_L -> /amplifier_left/CC_VAS
- R29 pad 1: GNDA -> Net-(R29-Pad1)
- R29 pad 2: Net-(Q10A-C) -> /amplifier_left/V_{bias}B
- R3 pad 1: Net-(K1-Pad10) -> /OUT_R
- R3 pad 2: GNDA -> /DC_LP_R
- R30 pad 1: -30V -> Net-(Q7A-B)
- R30 pad 2: Net-(Q12-B) -> +20Vreg
- R31 pad 1: Net-(Q11-B) -> /amplifier_left/CC_VAS
- R31 pad 2: Net-(Q10B-C) -> /amplifier_left/V_{bias}+
- R32 pad 1: Net-(R32-Pad1) -> -20Vreg
- R32 pad 2: Net-(Q11-B) -> Net-(Q9-E)
- R34 pad 1: Net-(Q10A-B) -> /amplifier_left/V_{OPS}-
- R34 pad 2: +30V -> Net-(D9-C/A)
- R35 pad 1: Net-(Q10B-C) -> /amplifier_left/V_{q}+
- R35 pad 2: Net-(Q11-C) -> Net-(D9-C/A)
- R36 pad 1: -30V -> Net-(D9-C/A)
- R36 pad 2: Net-(Q12-E) -> /amplifier_left/V_{q}-
- R38 pad 1: Net-(Q14-E) -> GND
- R38 pad 2: /AMP_L -> Net-(Q14A-B)
- R39 pad 1: Net-(Q15-E) -> GND
- R39 pad 2: /AMP_L -> Net-(Q15A-C)
- R4 pad 1: Net-(K1-Pad3) -> Net-(C14-Pad2)
- R4 pad 2: GNDA -> /AMP_L
- R40 pad 1: /AMP_L -> -20Vreg
- R40 pad 2: Net-(Q16-E) -> Net-(Q16A-E)
- R41 pad 1: /DAC_R -> Net-(Q14A-E)
- R41 pad 2: Net-(C24-Pad1) -> Net-(R41-Pad2)
- R42 pad 1: GNDA -> Net-(R41-Pad2)
- R42 pad 2: Net-(Q17A-B) -> /amplifier_right/CC_IPS
- R43 pad 1: GNDA -> Net-(Q15A-B)
- R43 pad 2: Net-(Q18A-C) -> +20Vreg
- R44 pad 1: -30V -> Net-(R44-Pad1)
- R44 pad 2: Net-(Q19A-E) -> /amplifier_right/CC_IPS
- R45 pad 1: Net-(Q17A-E) -> Net-(R44-Pad1)
- R45 pad 2: Net-(R45-Pad2) -> Net-(Q14B-E)
- R46 pad 1: Net-(R45-Pad2) -> -20Vreg
- R46 pad 2: Net-(Q18B-C) -> Net-(Q16B-E)
- R47 pad 1: Net-(Q18A-B) -> GND
- R47 pad 2: +30V -> /amplifier_right/FB
- R48 pad 1: Net-(R48-Pad1) -> /amplifier_right/FB
- R48 pad 2: Net-(Q18B-C) -> /AMP_R
- R49 pad 1: Net-(R48-Pad1) -> -20Vreg
- R49 pad 2: Net-(Q17B-E) -> Net-(Q17-E)
- R5 pad 2: +30V -> /AMP_R
- R50 pad 1: -30V -> GND
- R50 pad 2: Net-(Q19B-E) -> Net-(Q18A-C)
- R51 pad 1: GNDA -> /amplifier_right/V_{bias}B
- R51 pad 2: Net-(Q17B-B) -> /amplifier_right/CC_VAS
- R52 pad 1: Net-(Q17B-B) -> Net-(R52-Pad1)
- R52 pad 2: /AMP_R -> /amplifier_right/V_{bias}B
- R53 pad 1: GNDA -> Net-(Q18A-B)
- R53 pad 2: Net-(Q21A-C) -> +20Vreg
- R54 pad 1: -30V -> /amplifier_right/CC_VAS
- R54 pad 2: Net-(Q20-E) -> /amplifier_right/V_{bias}+
- R55 pad 1: Net-(Q22-B) -> -20Vreg
- R55 pad 2: Net-(Q21B-C) -> Net-(Q20-E)
- R56 pad 1: Net-(R56-Pad1) -> Net-(D10-C/A)
- R56 pad 2: Net-(Q22-B) -> /amplifier_right/V_{OPS}+
- R58 pad 1: Net-(Q21A-B) -> /amplifier_right/V_{q}+
- R58 pad 2: +30V -> Net-(D10-C/A)
- R59 pad 1: Net-(Q21B-C) -> Net-(D10-C/A)
- R59 pad 2: Net-(Q22-C) -> /amplifier_right/V_{q}-
- R7 pad 1: Net-(C13-Pad2) -> GND
- R7 pad 2: /OUT_L -> /AMP_R
- R8 pad 1: Net-(C14-Pad2) -> unconnected-(R8-Pad1)
- R8 pad 2: /OUT_R -> Net-(Q2A-B)
- R9 pad 1: Net-(Q4-B) -> Net-(Q2A-B)
- R9 pad 2: GNDA -> Net-(Q1-C)
- RV1 pad 1: Net-(C16-Pad1) -> /DAC_L
- RV1 pad 2: Net-(C17-Pad1) -> Net-(C18-Pad1)
- RV1 pad 3: GNDA -> GND
- RV1 pad 4: Net-(C24-Pad1) -> /DAC_R
- RV1 pad 6: GNDA -> GND
- U1 pad 1: Net-(U1-CPVDD) -> GND
- U1 pad 10: GNDA -> /SCK
- U1 pad 11: GNDA -> /DATA
- U1 pad 12: /SCK -> /LRCK
- U1 pad 13: /BCK -> unconnected-(U1-TSTO-Pad13)
- U1 pad 14: /DATA -> unconnected-(U1-TSTO-Pad14)
- U1 pad 15: /LRCK -> /DAC_L
- U1 pad 16: GNDA -> unconnected-(U1-~{AMUTEC}-Pad16)
- U1 pad 17: /SSPND -> Net-(U1-VBIAS)
- U1 pad 18: Net-(U1-LDOO) -> VBUS
- U1 pad 19: GNDA -> GND
- U1 pad 2: Net-(U1-CAPP) -> GND
- U1 pad 20: +3V3 -> Net-(U1-VQ)
- U1 pad 3: GNDA -> VBUS
- U1 pad 4: Net-(U1-CAPM) -> GND
- U1 pad 5: Net-(U1-VNEG) -> VBUS
- U1 pad 6: /DAC_L -> Net-(U1-VD_FILT)
- U1 pad 7: /DAC_R -> GND
- U1 pad 8: Net-(U1-AVDD) -> Net-(U1-POPGUARD/TSTO)
- U1 pad 9: GNDA -> VBUS
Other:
- board size 100 x 99 mm -> 90 x 99 mm
